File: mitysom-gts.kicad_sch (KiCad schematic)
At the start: 1 part, among them J100 Plug_Samtec_SEAM-50-02.0-L-08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

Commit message: [#100282] WIP: Clear ERC
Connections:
- no-connect marks 0 -> 24
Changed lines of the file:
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@@
 		)
+	)
+	(no_connect
+		(at 184.15 138.43)
+	)
+	(no_connect
+		(at 184.15 212.09)
+	)
+	(no_connect
+		(at 184.15 135.89)
+	)
+	(no_connect
+		(at 184.15 198.12)
+	)
+	(no_connect
+		(at 184.15 182.88)
+	)
+	(no_connect
+		(at 184.15 185.42)
+	)
+	(no_connect
+		(at 184.15 207.01)
+	)
+	(no_connect
+		(at 248.92 138.43)
+	)
+	(no_connect
+		(at 184.15 119.38)
+	)
+	(no_connect
+		(at 184.15 140.97)
+	)
+	(no_connect
+		(at 184.15 114.3)
+	)
+	(no_connect
+		(at 184.15 190.5)
+	)
+	(no_connect
+		(at 184.15 187.96)
+	)
+	(no_connect
+		(at 248.92 146.05)
+	)
+	(no_connect
+		(at 184.15 200.66)
+	)
+	(no_connect
+		(at 248.92 140.97)
+	)
+	(no_connect
+		(at 184.15 193.04)
+	)
+	(no_connect
+		(at 184.15 111.76)
+	)
+	(no_connect
+		(at 184.15 209.55)
+	)
+	(no_connect
+		(at 184.15 204.47)
+	)
+	(no_connect
+		(at 184.15 133.35)
+	)
+	(no_connect
+		(at 184.15 116.84)
+	)
+	(no_connect
+		(at 248.92 143.51)
+	)
+	(no_connect
+		(at 184.15 195.58)
 	)
 	(bus_entry

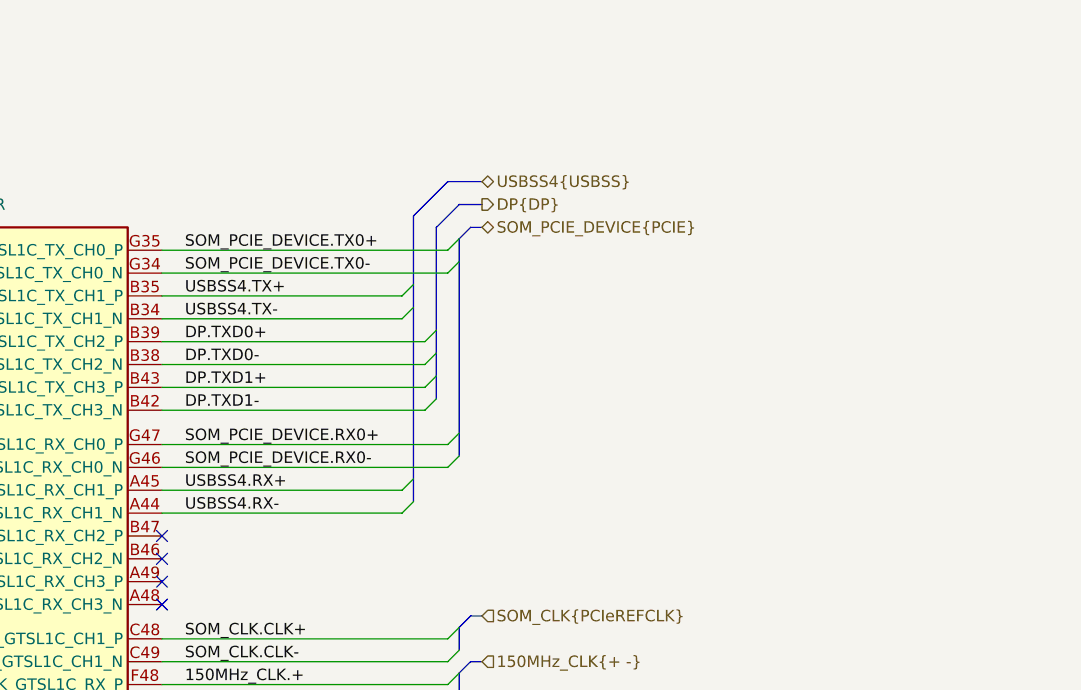
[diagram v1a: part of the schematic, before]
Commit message: [#100282] Clear ERC
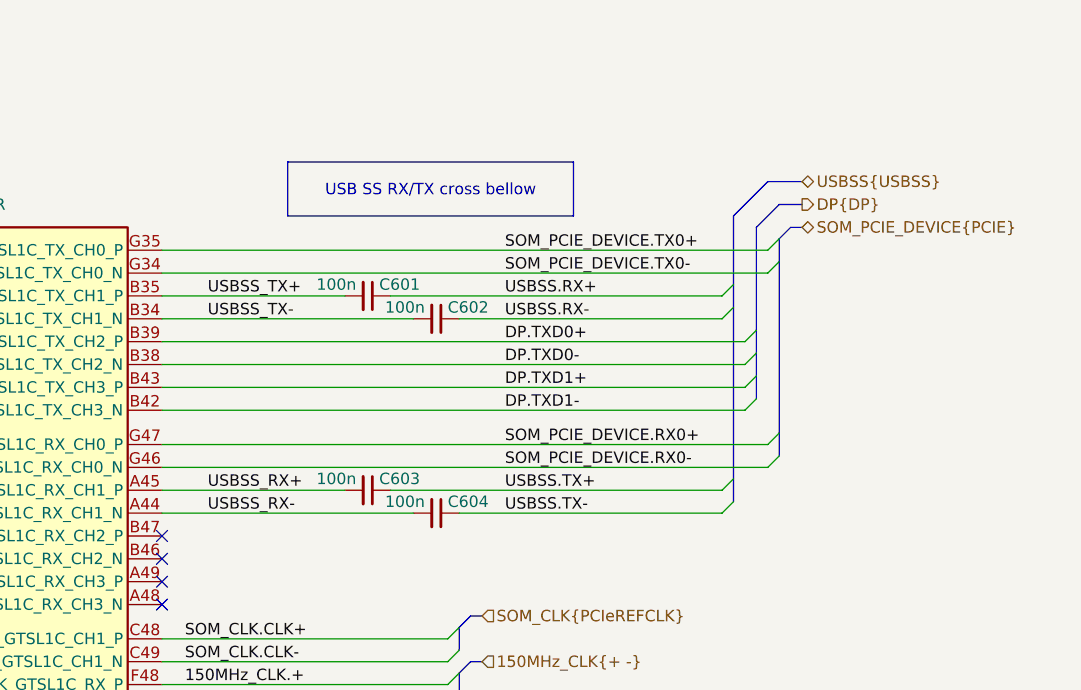
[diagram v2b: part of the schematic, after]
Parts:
- added C601, C602, C603, C604: C_100n_0402, antmicro-footprints:C_0402_1005Metric, symbol antmicroCapacitors0402:C_100n_0402
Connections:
- net USBSS4.RX+ renamed USBSS_RX+
- net USBSS_RX+: now also C603.2
- net USBSS4.RX- renamed USBSS_RX-
- net USBSS_RX-: now also C604.2
- net USBSS4.TX+ renamed USBSS_TX+
- net USBSS_TX+: now also C601.2
- net USBSS4.TX- renamed USBSS_TX-
- net USBSS_TX-: now also C602.2
- new net USBSS.RX+: C601.1
- new net USBSS.RX-: C602.1
- new net USBSS.TX+: C603.1
- new net USBSS.TX-: C604.1

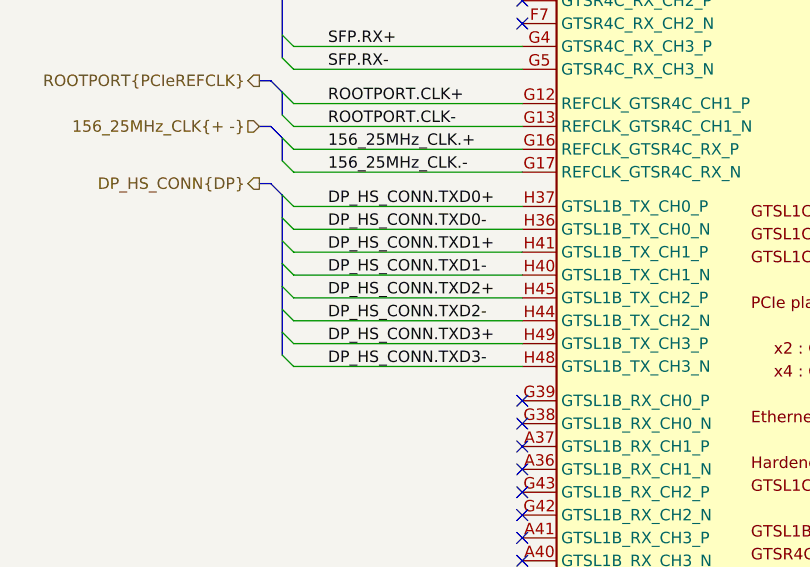
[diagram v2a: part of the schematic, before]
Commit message: [#100282] Remove unused DP lanes from schematic
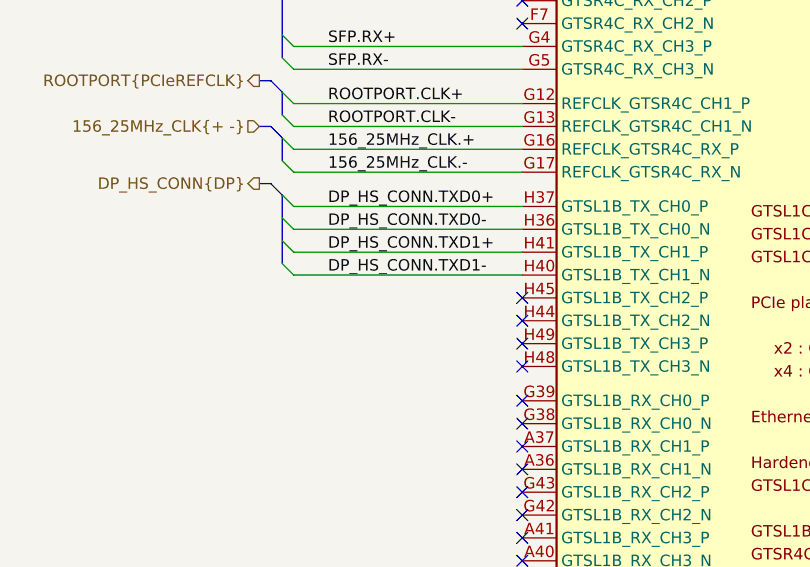
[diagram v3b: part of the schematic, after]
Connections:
- net DP_HS_CONN.TXD2+: no longer names the net of J100.H45 (GTSL1B_TX_CH2_P)
- net DP_HS_CONN.TXD2-: no longer names the net of J100.H44 (GTSL1B_TX_CH2_N)
- net DP_HS_CONN.TXD3+: no longer names the net of J100.H49 (GTSL1B_TX_CH3_P)
- net DP_HS_CONN.TXD3-: no longer names the net of J100.H48 (GTSL1B_TX_CH3_N)
- no-connect marks 24 -> 28
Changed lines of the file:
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@@
+	)
+	(no_connect
+		(at 184.15 179.07)
 	)
 	(no_connect
@@
 	)
 	(no_connect
+		(at 184.15 176.53)
+	)
+	(no_connect
 		(at 184.15 140.97)
 	)
@@
 	)
 	(no_connect
+		(at 184.15 171.45)
+	)
+	(no_connect
 		(at 184.15 111.76)
 	)
@@
 	(no_connect
 		(at 184.15 204.47)
+	)
+	(no_connect
+		(at 184.15 173.99)
 	)
 	(no_connect
@@
 	)
 	(bus_entry
-		(at 157.48 172.72)
-		(size 1.27 1.27)
-		(stroke
-			(width 0)
-			(type default)
-		)
-	)
-	(bus_entry
 		(at 157.48 165.1)
 		(size 1.27 1.27)
@@
 	)
 	(bus_entry
-		(at 157.48 175.26)
-		(size 1.27 1.27)
-		(stroke
-			(width 0)
-			(type default)
-		)
-	)
-	(bus_entry
 		(at 281.94 151.13)
 		(size -1.27 1.27)
@@
 	)
 	(bus_entry
-		(at 157.48 177.8)
-		(size 1.27 1.27)
-		(stroke
-			(width 0)
-			(type default)
-		)
-	)
-	(bus_entry
 		(at 160.02 129.54)
 		(size 1.27 1.27)
@@
 	)
 	(bus_entry
-		(at 157.48 170.18)
-		(size 1.27 1.27)
-		(stroke
-			(width 0)
-			(type default)
-		)
-	)
-	(bus_entry
 		(at 157.48 148.59)
 		(size 1.27 1.27)
@@
 	(bus
 		(pts
-			(xy 157.48 170.18) (xy 157.48 175.26)
-		)
-		(stroke
-			(width 0)
-			(type default)
-		)
-	)
-	(bus
-		(pts
 			(xy 281.94 151.13) (xy 281.94 148.59)
 		)
@@
 	(wire
 		(pts
-			(xy 158.75 171.45) (xy 184.15 171.45)
-		)
-		(stroke
-			(width 0)
-			(type default)
-		)
-	)
-	(wire
-		(pts
 			(xy 281.94 135.89) (xy 311.15 135.89)
 		)
@@
 	(bus
 		(pts
-			(xy 157.48 175.26) (xy 157.48 177.8)
-		)
-		(stroke
-			(width 0)
-			(type default)
-		)
-	)
-	(bus
-		(pts
 			(xy 156.21 158.75) (xy 157.48 160.02)
 		)
@@
 		)
 	)
-	(wire
-		(pts
-			(xy 158.75 179.07) (xy 184.15 179.07)
-		)
-		(stroke
-			(width 0)
-			(type default)
-		)
-	)
 	(bus
 		(pts
@@
 	(bus
 		(pts
-			(xy 157.48 160.02) (xy 157.48 162.56)
-		)
-		(stroke
-			(width 0)
-			(type default)
-		)
-	)
-	(bus
-		(pts
-			(xy 157.48 162.56) (xy 157.48 167.64)
-		)
-		(stroke
-			(width 0)
-			(type default)
-		)
-	)
-	(bus
-		(pts
 			(xy 312.42 102.87) (xy 312.42 134.62)
 		)
@@
 	(bus
 		(pts
-			(xy 157.48 167.64) (xy 157.48 170.18)
-		)
-		(stroke
-			(width 0)
-			(type default)
-		)
-	)
-	(bus
-		(pts
 			(xy 156.21 152.4) (xy 157.48 153.67)
 		)
@@
 	(wire
 		(pts
-			(xy 158.75 176.53) (xy 184.15 176.53)
-		)
-		(stroke
-			(width 0)
-			(type default)
-		)
-	)
-	(wire
-		(pts
 			(xy 158.75 124.46) (xy 184.15 124.46)
 		)
@@
 	(wire
 		(pts
-			(xy 158.75 173.99) (xy 184.15 173.99)
-		)
-		(stroke
-			(width 0)
-			(type default)
-		)
-	)
-	(wire
-		(pts
 			(xy 161.29 109.22) (xy 184.15 109.22)
 		)
@@
 		)
 	)
+	(bus
+		(pts
+			(xy 157.48 160.02) (xy 157.48 167.64)
+		)
+		(stroke
+			(width 0)
+			(type default)
+		)
+	)
 	(wire
 		(pts
@@
 			(width 0)
 			(type default)
-		)
-	)
-	(label "DP_HS_CONN.TXD2-"
-		(at 162.56 173.99 0)
-		(effects
-			(font
-				(size 1.27 1.27)
-			)
-			(justify left bottom)
 		)
 	)
@@
 		)
 	)
-	(label "DP_HS_CONN.TXD3-"
-		(at 162.56 179.07 0)
-		(effects
-			(font
-				(size 1.27 1.27)
-			)
-			(justify left bottom)
-		)
-	)
 	(label "DP_HS_CONN.TXD0+"
 		(at 162.56 161.29 0)
@@
 		)
 	)
-	(label "DP_HS_CONN.TXD2+"
-		(at 162.56 171.45 0)
-		(effects
-			(font
-				(size 1.27 1.27)
-			)
-			(justify left bottom)
-		)
-	)
 	(label "SOM_PCIE_DEVICE.RX0+"
 		(at 287.02 128.27 0)
@@
 	(label "150MHz_CLK.+"
 		(at 251.46 154.94 0)
-		(effects
-			(font
-				(size 1.27 1.27)
-			)
-			(justify left bottom)
-		)
-	)
-	(label "DP_HS_CONN.TXD3+"
-		(at 162.56 176.53 0)
 		(effects
 			(font
@@
 		(length 2.54)
 		(shape round)
-		(at 157.48 176.53 90)
+		(at 157.48 161.29 90)
 		(effects
 			(font
@@
 		)
 		(property "Net Class" "100Ohm-diff"
-			(at 154.178 176.53 0)
+			(at 154.178 161.29 0)
 			(show_name no)
 			(do_not_autoplace no)
@@
 		)
 		(property "Component Class" ""
-			(at 356.87 53.34 0)
+			(at 356.87 38.1 0)
 			(show_name no)
 			(do_not_autoplace no)

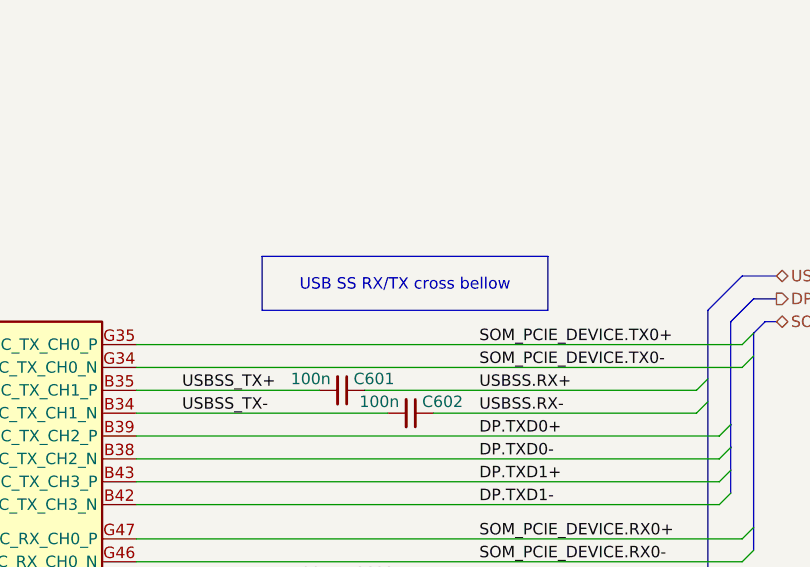
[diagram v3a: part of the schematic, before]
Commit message: [#100282] Add 1k resitor between DC_SCM_PRSNT pins
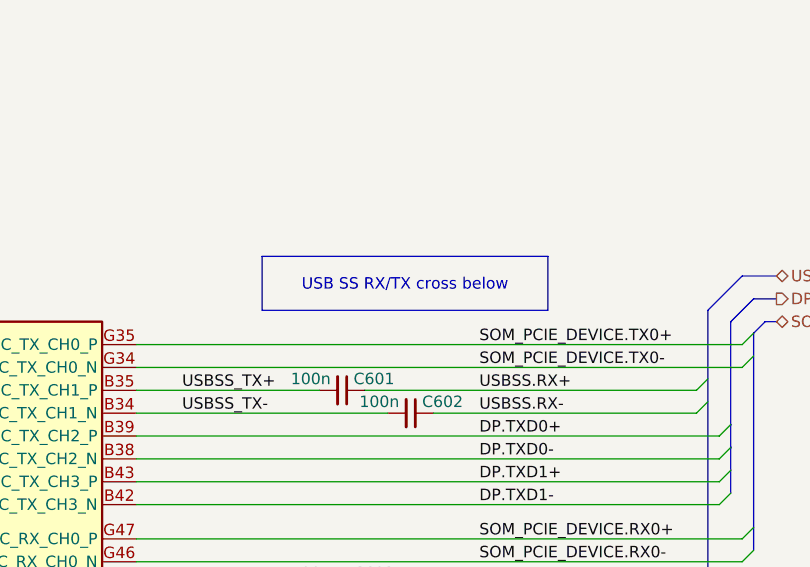
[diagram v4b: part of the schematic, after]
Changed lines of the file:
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@@
 		)
 	)
-	(text_box "USB SS RX/TX cross bellow"
+	(text_box "USB SS RX/TX cross below"
 		(exclude_from_sim no)
 		(at 262.89 96.8771 0)
